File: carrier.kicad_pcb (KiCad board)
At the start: 4 copper layers, 20.3 x 68.6 mm, 30 parts, among them J1 Conn_02x06_Odd_Even, J2 Conn_01x26, J3 Conn_01x26, U1 CARAVEL, U2 W25Q128JVS, U3 LP5907MFX-3.3, U4 LP5907MFX-1.8, U5 LP5907MFX-1.8, U6 LP5907MFX-3.3, X1 SG-5032CAN

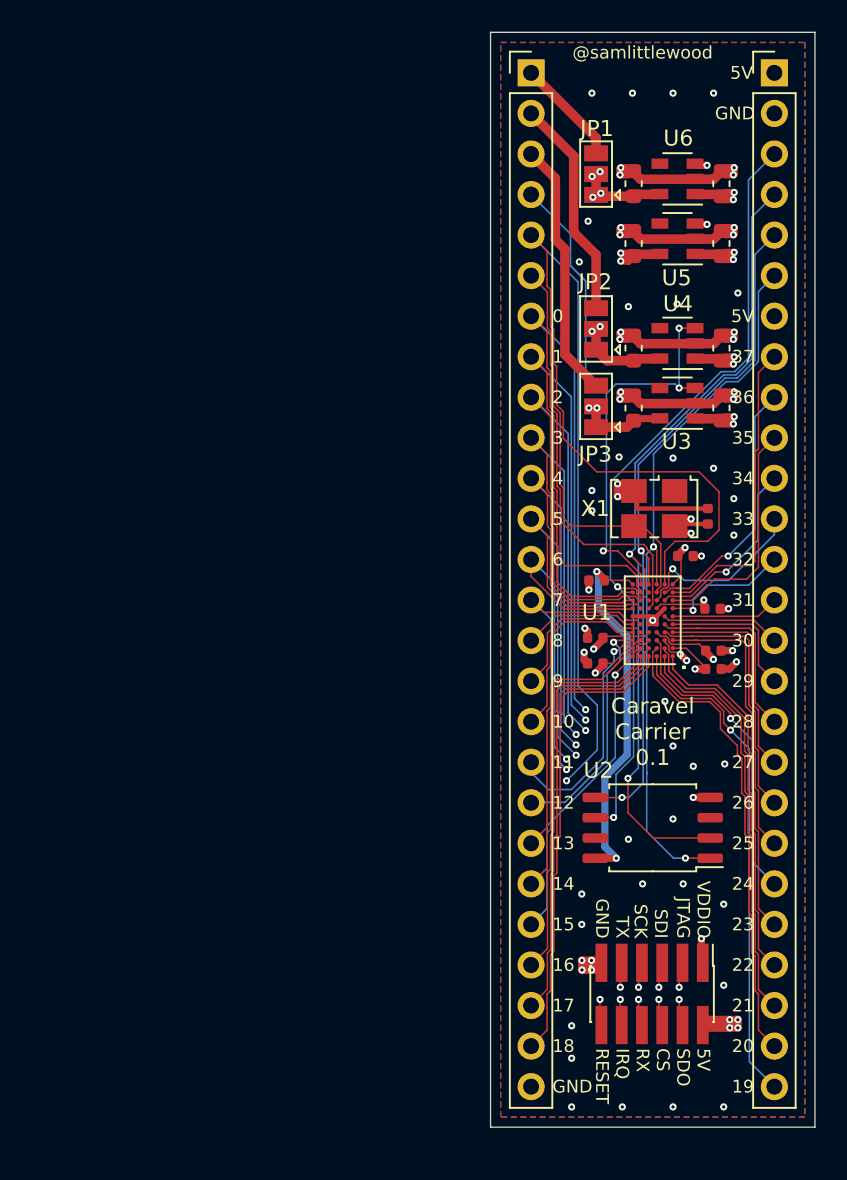
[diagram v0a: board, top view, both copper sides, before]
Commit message: Make wlcsp escape 3mil/3mil.
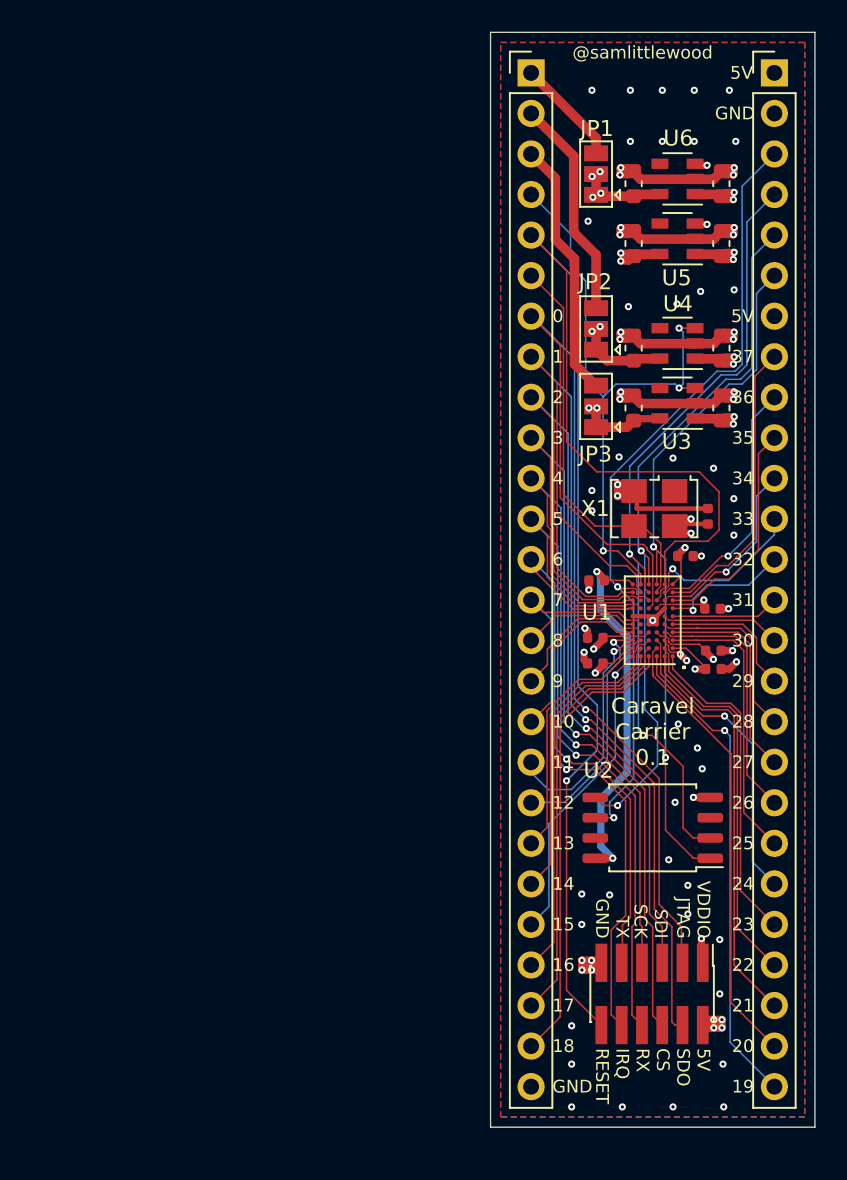
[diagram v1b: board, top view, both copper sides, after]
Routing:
- net mprj_io[0]: track 71.3 -> 67.5 mm, vias 2 -> 1
- net +5V: track 96.8 -> 93.3 mm
- net mprj_io[2]: track 59.2 -> 56.0 mm, vias 2 -> 1
- net mprj_io[4]: track 49.2 -> 46.3 mm, vias 2 -> 1
- net mprj_io[6]: track 39.0 -> 36.9 mm, vias 2 -> 1
- net mprj_io[7]: track 36.9 -> 38.6 mm, vias 2 -> 1
- net flash_io1: track 52.1 -> 50.6 mm
- net mprj_io[20]: track 29.5 -> 28.2 mm
- net mprj_io[1]: track 65.8 -> 64.6 mm, vias 2 -> 1
- net flash_io0: track 44.1 -> 45.2 mm
- net flash_csb: track 45.8 -> 44.7 mm
- net GND: track 61.0 -> 62.1 mm, vias 67 -> 73
- net mprj_io[18]: track 29.5 -> 28.6 mm
- net clock: track 25.9 -> 25.1 mm
- net mprj_io[17]: track 27.5 -> 26.6 mm
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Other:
- net class Default: clearance 0.1 -> 0.0762; trace_width 0.1 -> 0.1016
- net class Fanout: clearance 0.05 -> 0.0762; trace_width 0.1 -> 0.0762
- rule trace_clearance: 0.1 -> 0.0762
- rule trace_min: 0.1 -> 0.0762

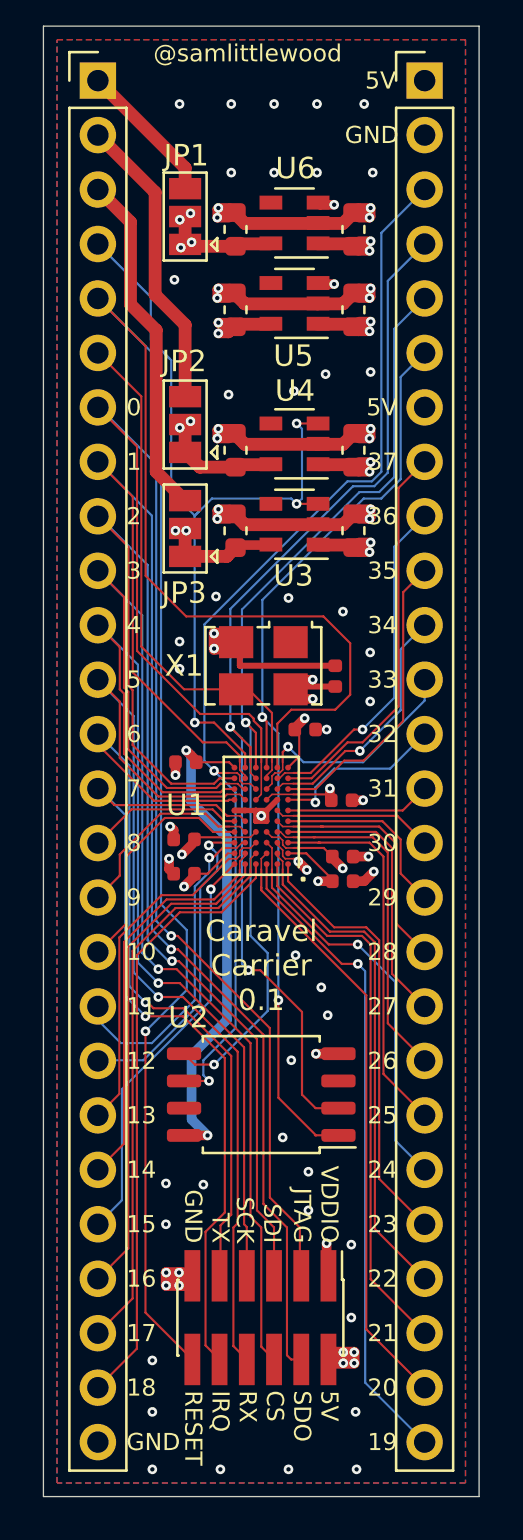
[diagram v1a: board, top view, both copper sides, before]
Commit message: Made rest of board 4mil/4mil.
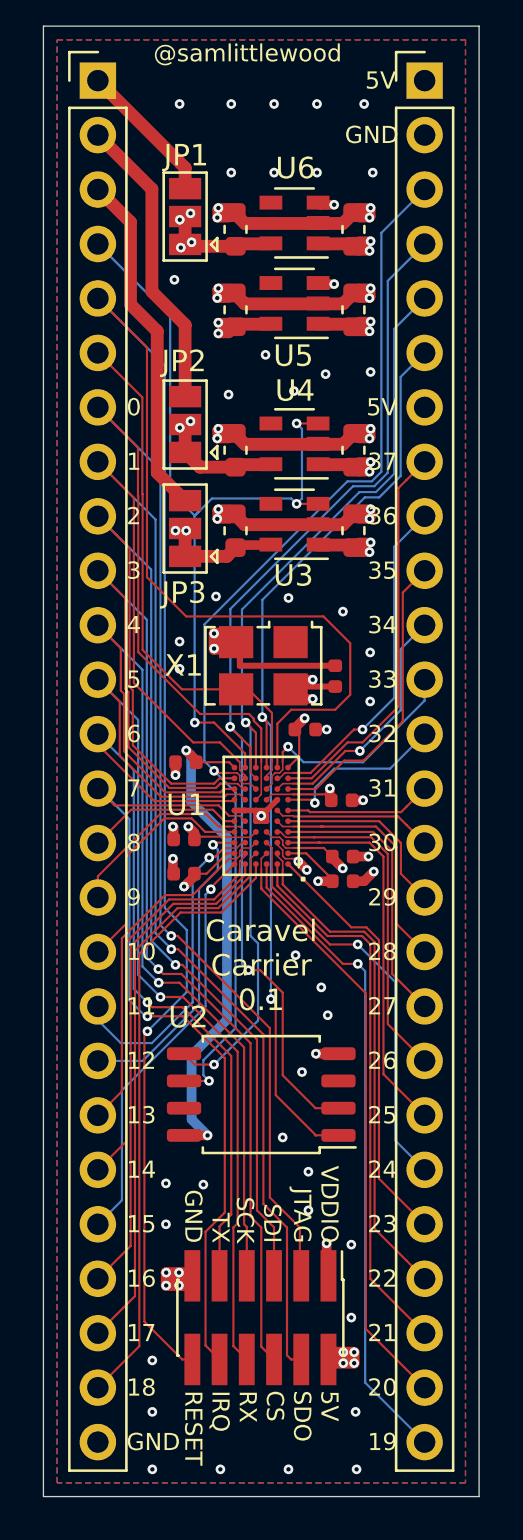
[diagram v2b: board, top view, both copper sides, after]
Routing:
- net vdda1: track 38.9 -> 40.4 mm
- net gpio: track 40.5 -> 39.2 mm
- net GND: track 62.1 -> 61.9 mm, vias 73 -> 74

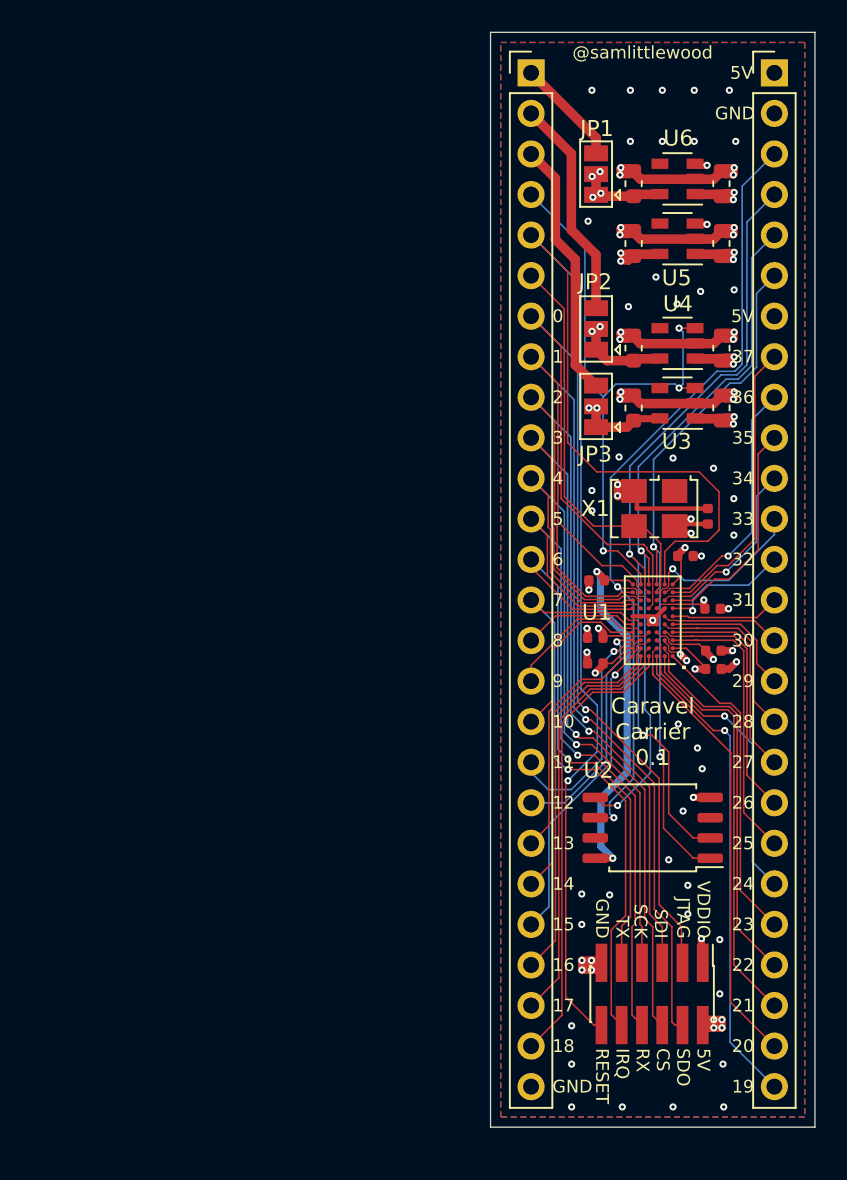
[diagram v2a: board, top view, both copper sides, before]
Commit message: updating for vga clock
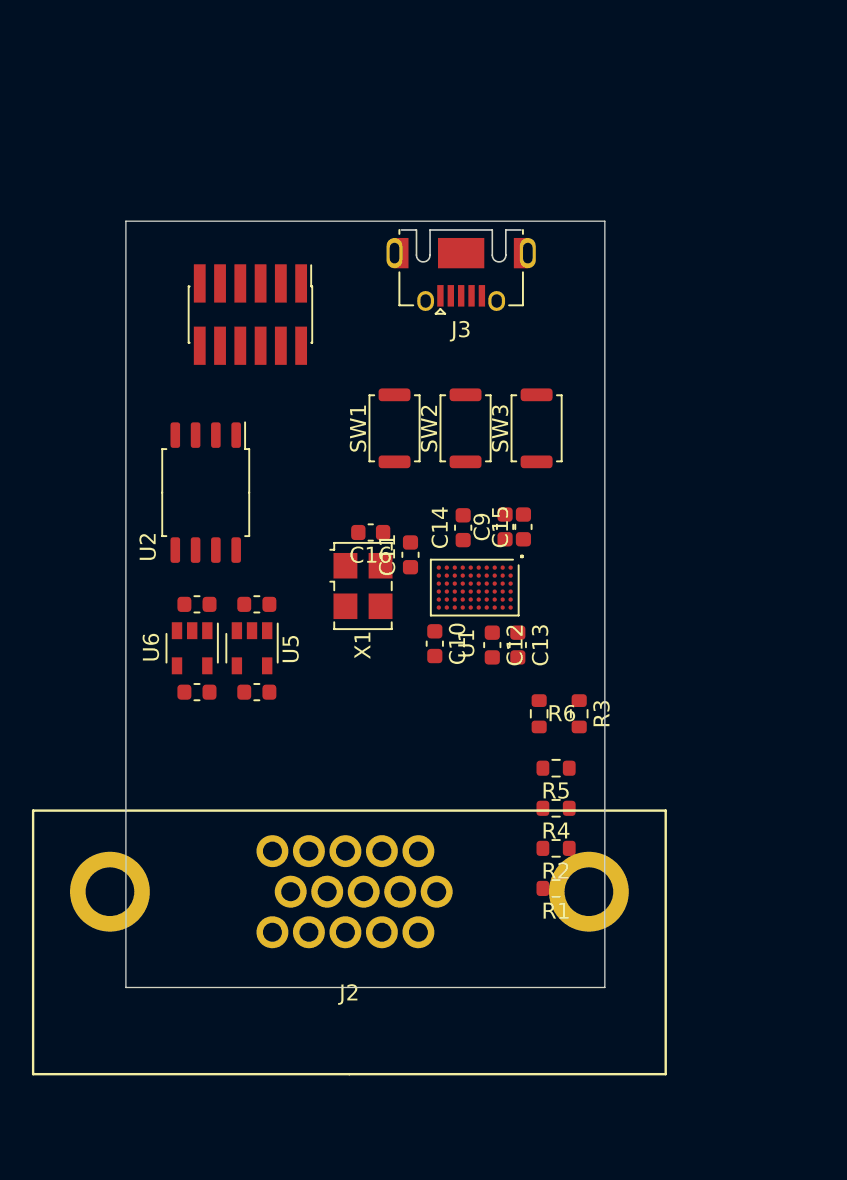
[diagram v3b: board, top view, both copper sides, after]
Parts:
- removed C2, C6: 1u, Capacitor_SMD:C_0603_1608Metric
- removed C4, C8: 4u7, Capacitor_SMD:C_0603_1608Metric
- removed G***: TEAPOT, carrier:sketch_teapot
- removed JP1: VIO_SEL, Jumper:SolderJumper-3_P1.3mm_Bridged12_Pad1.0x1.5mm
- removed JP2: 1V8_SEL, Jumper:SolderJumper-3_P1.3mm_Bridged12_Pad1.0x1.5mm
- removed JP3: 3V3_SEL, Jumper:SolderJumper-3_P1.3mm_Bridged12_Pad1.0x1.5mm
- removed U3: LP5907MFX-3.3, Package_TO_SOT_SMD:SOT-23-5
- removed U4: LP5907MFX-1.8, Package_TO_SOT_SMD:SOT-23-5
- added R1: R, Resistor_SMD:R_0603_1608Metric, F.Cu at (62.7, 96.8)
- added R2: R, Resistor_SMD:R_0603_1608Metric, F.Cu at (62.7, 94.3)
- added R3: R, Resistor_SMD:R_0603_1608Metric, F.Cu at (64.1, 85.9)
- added R4: R, Resistor_SMD:R_0603_1608Metric, F.Cu at (62.7, 91.8)
- added R5: R, Resistor_SMD:R_0603_1608Metric, F.Cu at (62.7, 89.3)
- added R6: R, Resistor_SMD:R_0603_1608Metric, F.Cu at (61.6, 85.9)
- added SW1: SW_Push_hrs, Button_Switch_SMD:SW_Push_SPST_NO_Alps_SKRK, F.Cu at (52.6, 68.0)
- added SW2: SW_Push_min, Button_Switch_SMD:SW_Push_SPST_NO_Alps_SKRK, F.Cu at (57.0, 68.0)
- added SW3: SW_Push_sec, Button_Switch_SMD:SW_Push_SPST_NO_Alps_SKRK, F.Cu at (61.5, 68.0)
- C10, C11, C12, C13, C14, C15, C16, C9: footprint Capacitor_SMD:C_0402_1005Metric -> Capacitor_SMD:C_0603_1608Metric
- J2: value Conn_01x26 -> DB15_Female_HighDensity; footprint Connector_PinHeader_2.54mm:PinHeader_1x26_P2.54mm_Vertical -> carrier:db15
- J3: value Conn_01x26 -> USB_B_Micro; footprint Connector_PinHeader_2.54mm:PinHeader_1x26_P2.54mm_Vertical -> Connector_USB:USB_Micro-AB_Molex_47590-0001
- moved J2 52.5 mm to (49.7, 97.0), turned to 180 degrees
- moved J1 49.4 mm to (43.5, 60.9)
- moved U6 42.3 mm to (39.9, 81.8), turned to 270 degrees
- moved C5 42.1 mm to (40.2, 79.0), turned to 180 degrees
- moved C7 42.0 mm to (40.2, 84.5), turned to 180 degrees
- moved U5 37.0 mm to (43.6, 81.8), turned to 270 degrees
- moved C1 36.8 mm to (43.9, 79.0), turned to 180 degrees
- moved C3 36.7 mm to (43.9, 84.5), turned to 180 degrees
- moved U2 35.0 mm to (40.7, 72.0), turned to 270 degrees
- moved J3 22.6 mm to (56.7, 57.0), turned to 180 degrees
- moved C16 21.1 mm to (51.1, 74.5), turned to 180 degrees
- moved X1 18.9 mm to (50.6, 77.9), turned to 270 degrees
- moved C11 17.2 mm to (53.6, 75.9), turned to 90 degrees
- moved C14 16.4 mm to (56.9, 74.2), turned to 90 degrees
- moved C9 15.2 mm to (59.5, 74.2), turned to 90 degrees
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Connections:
- C12 pad 1: vdda1 -> vccd
- C13 pad 1: vccd1 -> vccd
- C14 pad 1: vdda1 -> vccd
- C15 pad 1: vccd1 -> vccd
- C9 pad 1: vddio -> vdda
- J1 pad 1: vddio -> vdda
- J2 pad 1: ext_vddio -> /red
- J2 pad 10: mprj_io[3] -> GND
- J2 pad 11: mprj_io[4] -> Net-(J2-Pad11)
- J2 pad 12: mprj_io[5] -> Net-(J2-Pad12)
- J2 pad 13: mprj_io[6] -> /hsync
- J2 pad 14: mprj_io[7] -> /vsync
- J2 pad 15: mprj_io[8] -> Net-(J2-Pad15)
- J2 pad 2: ext_1v8 -> /green
- J2 pad 3: ext_3v3 -> /blue
- J2 pad 4: gpio -> Net-(J2-Pad4)
- J2 pad 5: resetb -> GND
- J2 pad 6: clock -> GND
- J2 pad 7: mprj_io[0] -> GND
- J2 pad 8: mprj_io[1] -> GND
- J2 pad 9: mprj_io[2] -> Net-(J2-Pad9)
- J3 pad 2: GND -> Net-(J3-Pad2)
- J3 pad 3: flash_clk -> Net-(J3-Pad3)
- J3 pad 4: flash_io1 -> Net-(J3-Pad4)
- J3 pad 5: flash_io0 -> GND
- J3 pad 6: flash_csb -> Net-(J3-Pad6)
- U1 pad A2: vccd1 -> vccd
- U1 pad C4: vddio -> vdda
- U1 pad C7: vdda1 -> vccd
- U1 pad D4: vdda1 -> vccd
- U1 pad F2: vccd1 -> vccd
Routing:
- net +5V: track 93.3 -> 0.00 mm, vias 14 -> 0
- net resetb: track 86.3 -> 0.00 mm, vias 1 -> 0
- net vdda: track 76.0 -> 0.00 mm, vias 6 -> 0
- net mprj_io[0]: track 67.5 -> 0.00 mm, vias 1 -> 0
- net mprj_io[1]: track 64.7 -> 0.00 mm, vias 1 -> 0
- net GND: track 61.9 -> 0.00 mm, vias 74 -> 0
- net vddio: track 58.0 -> 0.00 mm, vias 4 -> 0
- net mprj_io[2]: track 56.0 -> 0.00 mm, vias 1 -> 0
- net mprj_io[3]: track 55.9 -> 0.00 mm, vias 1 -> 0
- net flash_clk: track 51.4 -> 0.00 mm, vias 2 -> 0
- net flash_io1: track 50.6 -> 0.00 mm, vias 2 -> 0
- net mprj_io[4]: track 46.2 -> 0.00 mm, vias 1 -> 0
- net mprj_io[5]: track 46.1 -> 0.00 mm, vias 1 -> 0
- net flash_io0: track 44.8 -> 0.00 mm, vias 2 -> 0
- net flash_csb: track 44.6 -> 0.00 mm, vias 2 -> 0
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- removed copper zone on B.Cu, net GND
- removed copper zone on F.Cu, net GND
- removed copper zone on In1.Cu, net GND
- removed copper zone on In2.Cu, net GND
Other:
- board size 20.3 x 68.6 mm -> 30 x 48 mm
- board text removed: "0"
- board text removed: "1"
- board text removed: "10"
- board text removed: "11"
- board text removed: "12"
- board text removed: "13"
- board text removed: "14"
- board text removed: "15"
- board text removed: "16"
- board text removed: "17"
- board text removed: "18"
- board text removed: "19"
- board text removed: "2"
- board text removed: "20"
- board text removed: "21"
- board text removed: "22"
- board text removed: "23"
- board text removed: "24"
- board text removed: "25"
- board text removed: "26"
- board text removed: "27"
- board text removed: "28"
- board text removed: "29"
- board text removed: "3"
- board text removed: "30"
- board text removed: "31"
- board text removed: "32"
- board text removed: "33"
- board text removed: "34"
- board text removed: "35"
- board text removed: "36"
- board text removed: "37"
- board text removed: "4"
- board text removed: "5"
- board text removed: "5V"
- board text removed: "6"
- board text removed: "7"
- board text removed: "8"
- board text removed: "9"
- board text removed: "@samlittlewood"
- board text removed: "CS"
- board text removed: "Caravel Carrier 0.1"
- board text removed: "GND"
- board text removed: "IRQ"
- board text removed: "JTAG"
- board text removed: "RESET"
- board text removed: "RX"
- board text removed: "SCK"
- board text removed: "SDI"
- board text removed: "SDO"
- board text removed: "TX"
- board text removed: "VDDIO"
- board text removed: "clock"
- board text removed: "ext_1v8"
- board text removed: "ext_3v3"
- board text removed: "ext_vddio"
- board text removed: "flash_clk"
- board text removed: "flash_csb"
- board text removed: "flash_io0"
- board text removed: "flash_io1"
- board text removed: "gpio"
- board text removed: "https://github.com/samlittlewood/caravel_carrier"
- board text removed: "resetb"

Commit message: updated pcb
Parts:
- removed C12, C13, C14, C15: 22n, Capacitor_SMD:C_0603_1608Metric
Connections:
- net gpio renamed Net-(U1-PadE10)
- net mprj_io[19] renamed Net-(U1-PadC1)
- net mprj_io[20] renamed Net-(U1-PadC2)
- net mprj_io[21] renamed Net-(U1-PadB1)
- net mprj_io[22] renamed Net-(U1-PadB2)
- net mprj_io[23] renamed Net-(U1-PadA1)
- net mprj_io[24] renamed Net-(U1-PadC3)
- net mprj_io[25] renamed Net-(U1-PadA3)
- net mprj_io[26] renamed Net-(U1-PadB4)
- net mprj_io[27] renamed Net-(U1-PadA4)
- net mprj_io[28] renamed Net-(U1-PadB5)
- net mprj_io[29] renamed Net-(U1-PadA5)
- net mprj_io[30] renamed Net-(U1-PadB6)
- net mprj_io[31] renamed Net-(U1-PadA6)
- net mprj_io[32] renamed Net-(U1-PadA7)
- net mprj_io[33] renamed Net-(U1-PadC8)
- net mprj_io[34] renamed Net-(U1-PadB8)
- net mprj_io[35] renamed Net-(U1-PadA8)
- net mprj_io[36] renamed Net-(U1-PadB9)
- net mprj_io[37] renamed Net-(U1-PadA9)
- U1 pad A2: vccd -> Net-(U1-PadA2)
- U1 pad C7: vccd -> Net-(U1-PadC7)
- U1 pad D4: vccd -> Net-(U1-PadD4)
